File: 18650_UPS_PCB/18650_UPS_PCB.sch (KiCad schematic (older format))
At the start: 54 parts, among them J1 USB_B_Micro, J2 Conn_02x04_Odd_Even, J3 USB_A, SW1 SW_SPDT, SW2 ALPSALPINE_SKRHADE011, SW3 SW_SPDT, SW4 SW_SPDT, SW5 SW_SPDT, U1 STLINK-V3MINI, U10 LR9102G-xx, U2 R5478, U3 STC4054, U4 FS8205A, U5 ME2188Cxx, U6 XC9236Axx, U7 INA219AxD, U8 SSD1306_128_32, U9 STM32F030F4Px

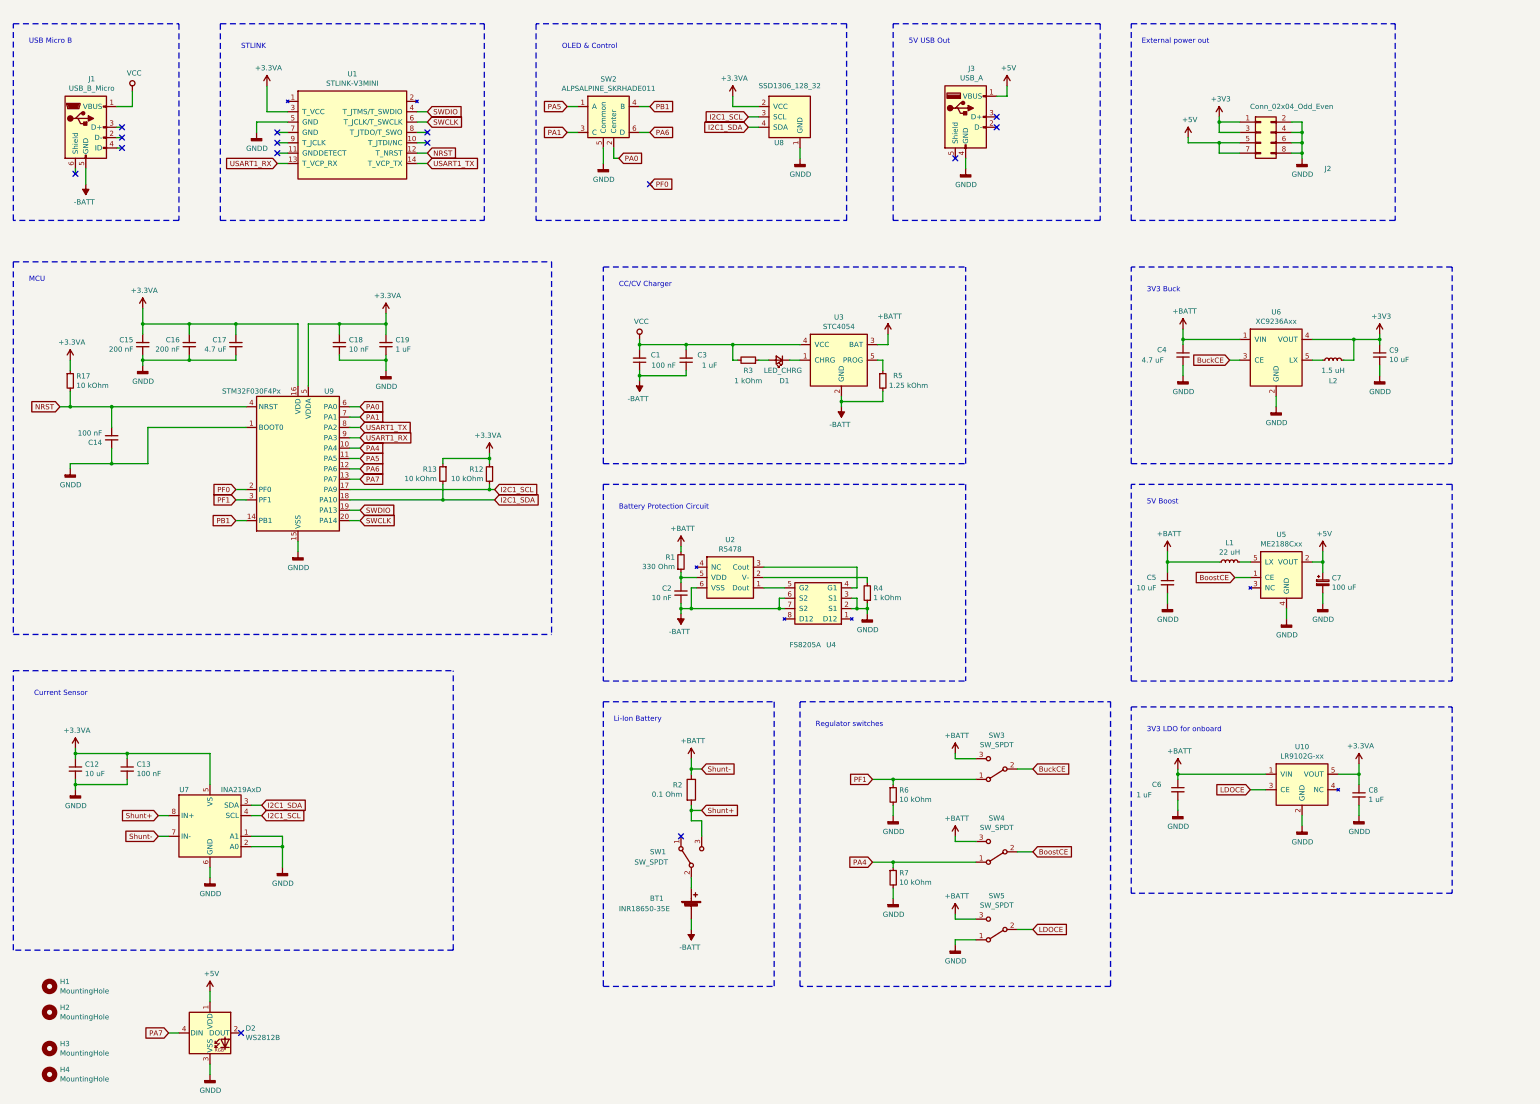
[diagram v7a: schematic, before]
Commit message: base for v2 with new bms and sense ic
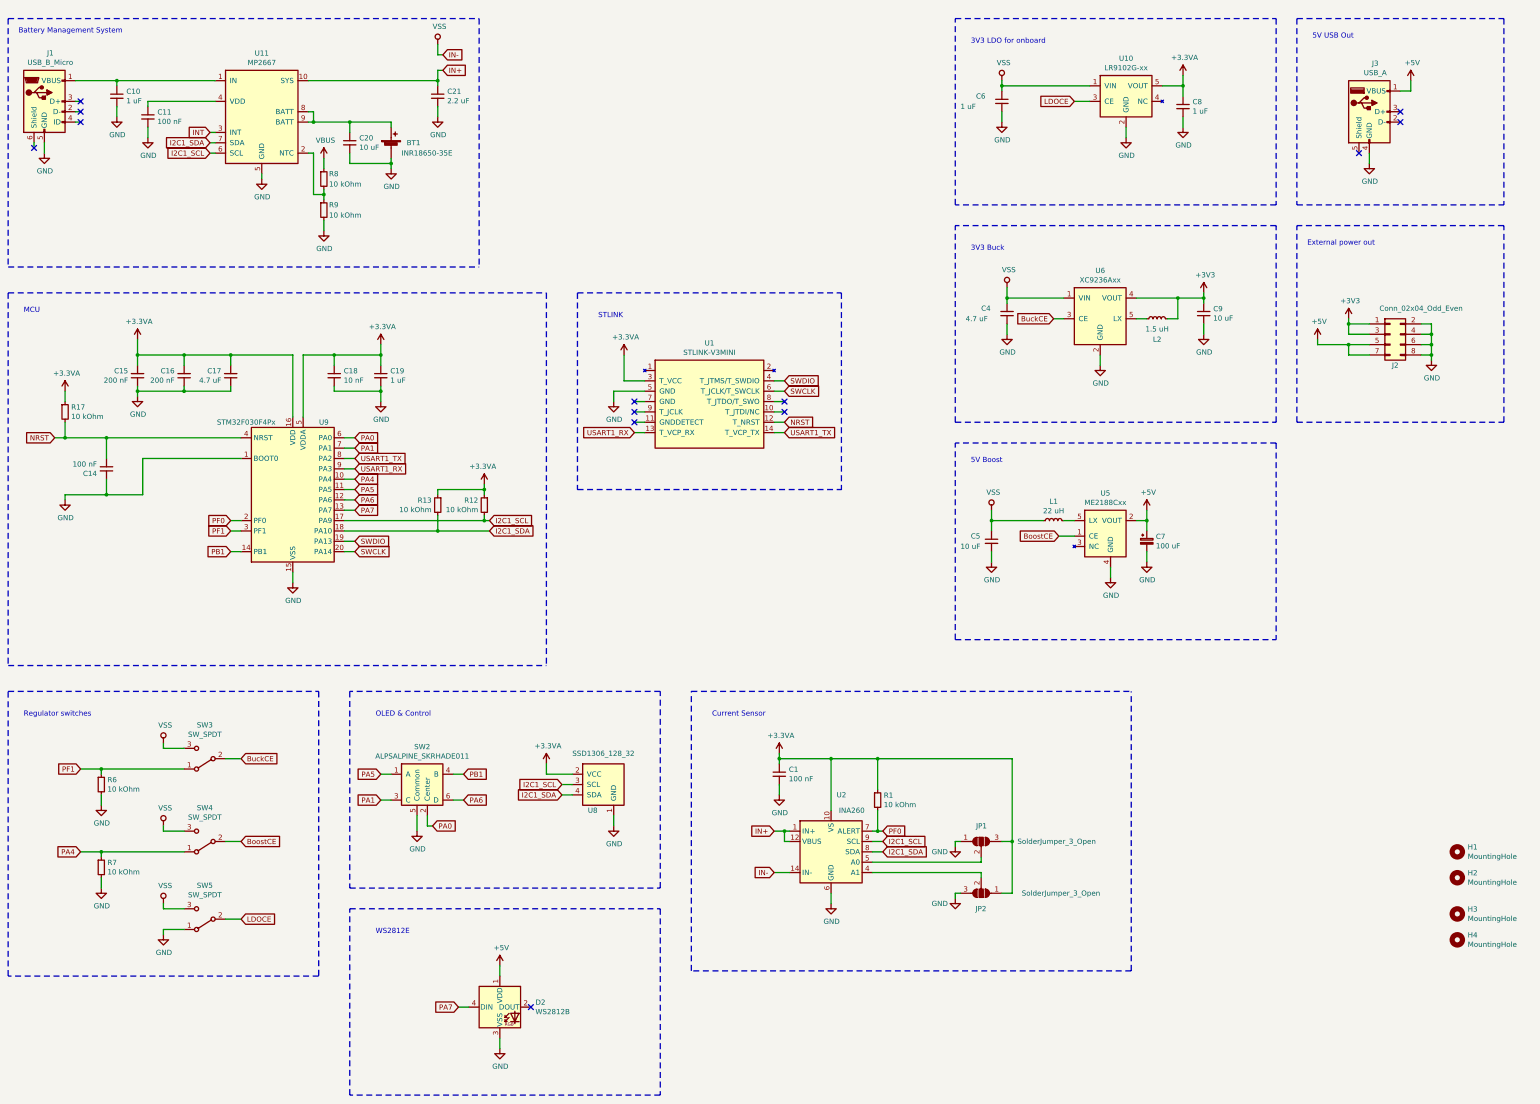
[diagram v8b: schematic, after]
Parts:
- removed C12: 10 uF, Capacitor_SMD:C_0603_1608Metric, symbol Device:C_Small
- removed C13: 100 nF, Capacitor_SMD:C_0603_1608Metric, symbol Device:C_Small
- removed C2: 10 nF, Capacitor_SMD:C_0603_1608Metric, symbol Device:C_Small
- removed C3: 1 uF, Capacitor_SMD:C_0603_1608Metric, symbol Device:C_Small
- removed D1: LED_CHRG, LED_SMD:LED_0603_1608Metric, symbol Device:LED_Small
- removed R2: 0.1 Ohm, Resistor_SMD:R_2512_6332Metric, symbol Device:R
- removed R3, R4: 1 kOhm, Resistor_SMD:R_0603_1608Metric, symbol Device:R_Small
- removed R5: 1.25 kOhm, Resistor_SMD:R_0603_1608Metric, symbol Device:R_Small
- removed SW1: SW_SPDT, CUSTOM_FOOTPRINTS:ALPS_SPEF210101, symbol Switch:SW_SPDT
- removed U2: R5478, Package_TO_SOT_SMD:SOT-23-6, symbol CUSTOM_PARTS:R5478
- removed U3: STC4054, Package_TO_SOT_SMD:TSOT-23-5, symbol CUSTOM_PARTS:STC4054
- removed U4: FS8205A, Package_SO:TSSOP-8_4.4x3mm_P0.65mm, symbol CUSTOM_PARTS:FS8205A
- removed U7: INA219AxD, Package_SO:SOIC-8_3.9x4.9mm_P1.27mm, symbol Analog_ADC:INA219AxD
- added C10: 1 uF, Capacitor_SMD:C_0603_1608Metric, symbol Device:C_Small
- added C11: 100 nF, Capacitor_SMD:C_0603_1608Metric, symbol Device:C_Small
- added C20: 10 uF, Capacitor_SMD:C_0603_1608Metric, symbol Device:C_Small
- added C21: 2.2 uF, Capacitor_SMD:C_0603_1608Metric, symbol Device:C_Small
- added JP1, JP2: SolderJumper_3_Open, Jumper:SolderJumper-3_P1.3mm_Open_RoundedPad1.0x1.5mm, symbol Jumper:SolderJumper_3_Open
- added R8, R9: 10 kOhm, Resistor_SMD:R_0603_1608Metric, symbol Device:R_Small
- added U11: MP2667, CUSTOM_FOOTPRINTS:QFN-10-MP2667, symbol CUSTOM_PARTS:MP2667
- added U2: INA260, Package_SO:TSSOP-16_4.4x5mm_P0.65mm, symbol Sensor:INA260
- R1: value 330 Ohm -> 10 kOhm
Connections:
- net GNDD is gone; now on net GND: C14.1, C15.1, C16.1, C17.1, C18.2, C19.2, C4.2, C5.2, C6.2, C7.2, C8.2, C9.2, D2.3 (VSS), J2.2 (Pin_2), J2.4 (Pin_4), J2.6 (Pin_6), J2.8 (Pin_8), J3.4 (GND), R6.2, R7.2, SW2.5 (Common), SW5.1 (A), U1.5 (GND), U10.2 (GND), U5.4 (GND), U6.2 (GND), U8.1 (GND), U9.1 (BOOT0), U9.15 (VSS)
- net +3.3VA: now also C1.1, R1.1, JP1.3 (B), JP2.1 (A), U2.10 (VS)
- net I2C1_SCL: now also U11.6 (SCL), U2.9 (SCL)
- net I2C1_SDA: now also U11.7 (SDA), U2.8 (SDA)
- net PF0: now also R1.2, U2.7 (ALERT)
- net at BT1.1 (+): now also C20.1, U11.8 (BATT), U11.9 (BATT)
- net +BATT renamed VSS
- net VSS: now also U2.14 (IN-), U2.15 (IN-), U2.16 (IN-); no longer R1.2
- net -BATT renamed GND
- net GND: now also C1.2, C10.2, C11.2, C20.2, C21.2, JP1.1 (A), JP2.3 (B), R9.2, U11.5 (GND), U2.11 (GND), U2.6 (GND); no longer C1.1
- net VCC: no longer names the net of J1.1 (VBUS)
- net VCC: now also C10.1, U11.1 (IN); no longer C1.2
- new net: R8.2, R9.1, U11.2 (NTC)
- new net: C11.1, U11.4 (VDD)
- new net: JP2.2 (C), U2.4 (A1)
- new net: JP1.2 (C), U2.5 (A0)
- new net IN+: C21.1, U11.10 (SYS), U2.1 (IN+), U2.12 (VBUS), U2.2 (IN+), U2.3 (IN+)
- new net INT: U11.3 (INT)
- new net VBUS: R8.1
- no-connect marks 15 -> 13
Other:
- note added: "Battery Management System"
- note added: "WS2812E"
- note removed: "Battery Protection Circuit"
- note removed: "CC/CV Charger"
- note removed: "Li-Ion Battery"
- note removed: "USB Micro B"
- moved on the sheet: BT1, C14, C15, C16, C17, C18, C19, C4, C5, C6, C7, C8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
